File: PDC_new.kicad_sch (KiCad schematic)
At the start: 17 parts, among them J1 Conn_01x02, J10 Conn_01x02, J2 Conn_01x02, J3 Conn_01x02, J4 Conn_01x02, J5 Conn_01x02, J6 Conn_01x02, J7 Conn_01x02, J8 Conn_01x02, J9 Conn_01x02

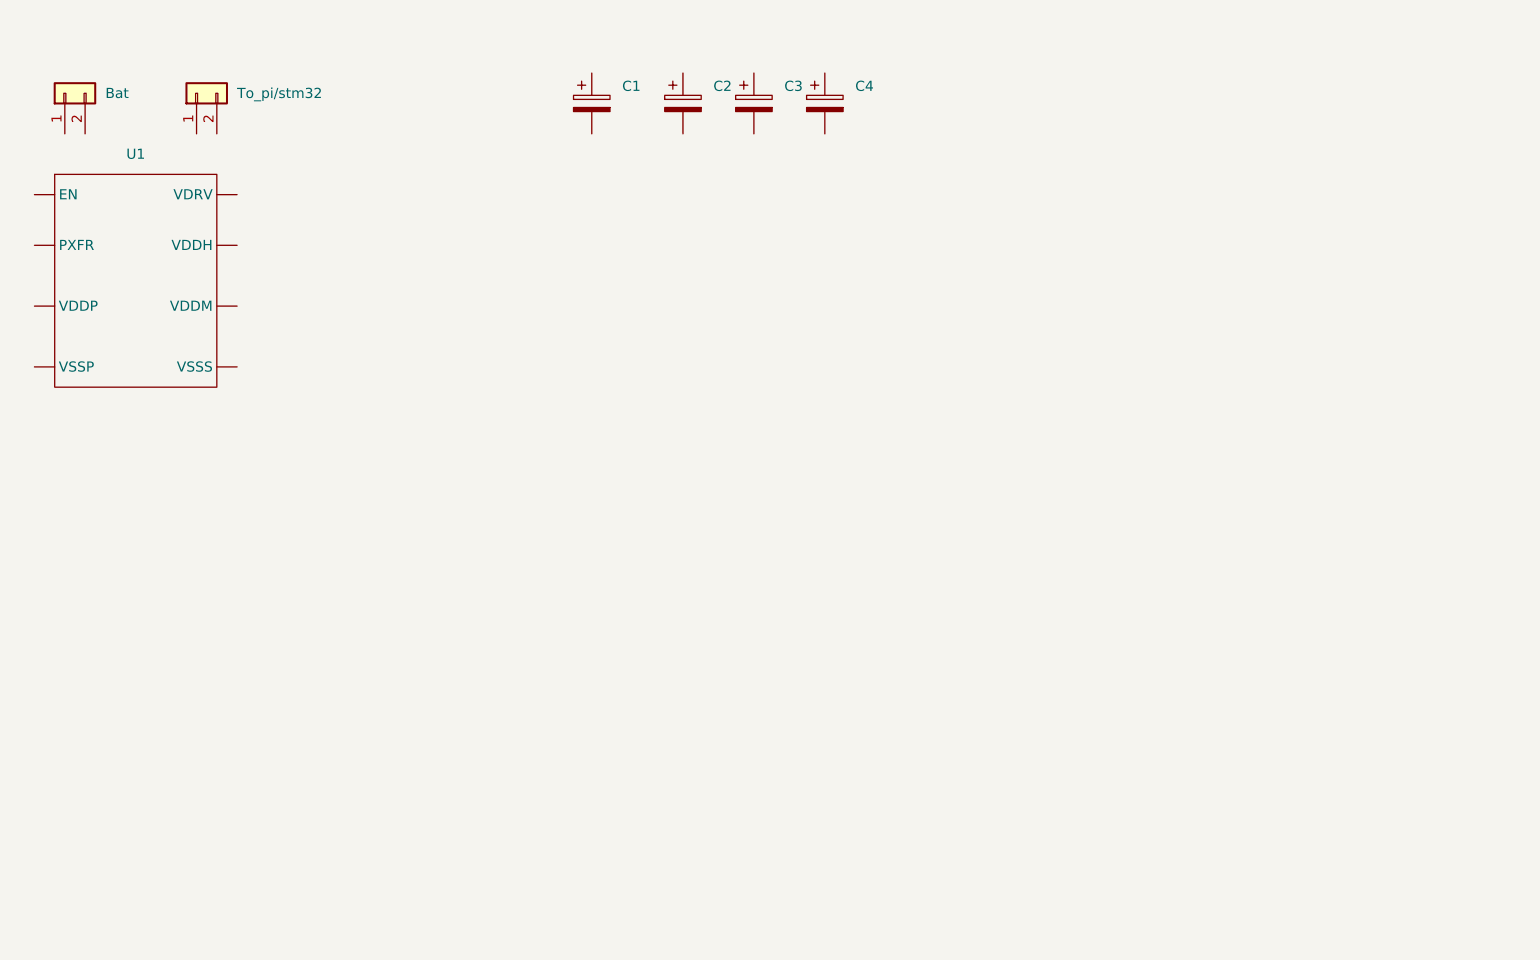
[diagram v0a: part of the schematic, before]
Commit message: Update PDC schematic with protection, timing and control logic
- Add XT90PW-F power input connector and SMCJ54CA-13-F TVS diode
- Add 3x TPSI3050-Q1 isolated switch drivers
- Add NE555 timer, LM393 comparator and 74HC14/74HC74/74LS08 logic
- Add Schottky diode and update connector/capacitor wiring
- Update project designators (C1-4, D1-2, J1-12, U1-8)

KiCad local files (.kicad_prl, backups, .history) remain ignored.

Co-Authored-By: Claude Opus 5.5 <noreply@anthropic.com>
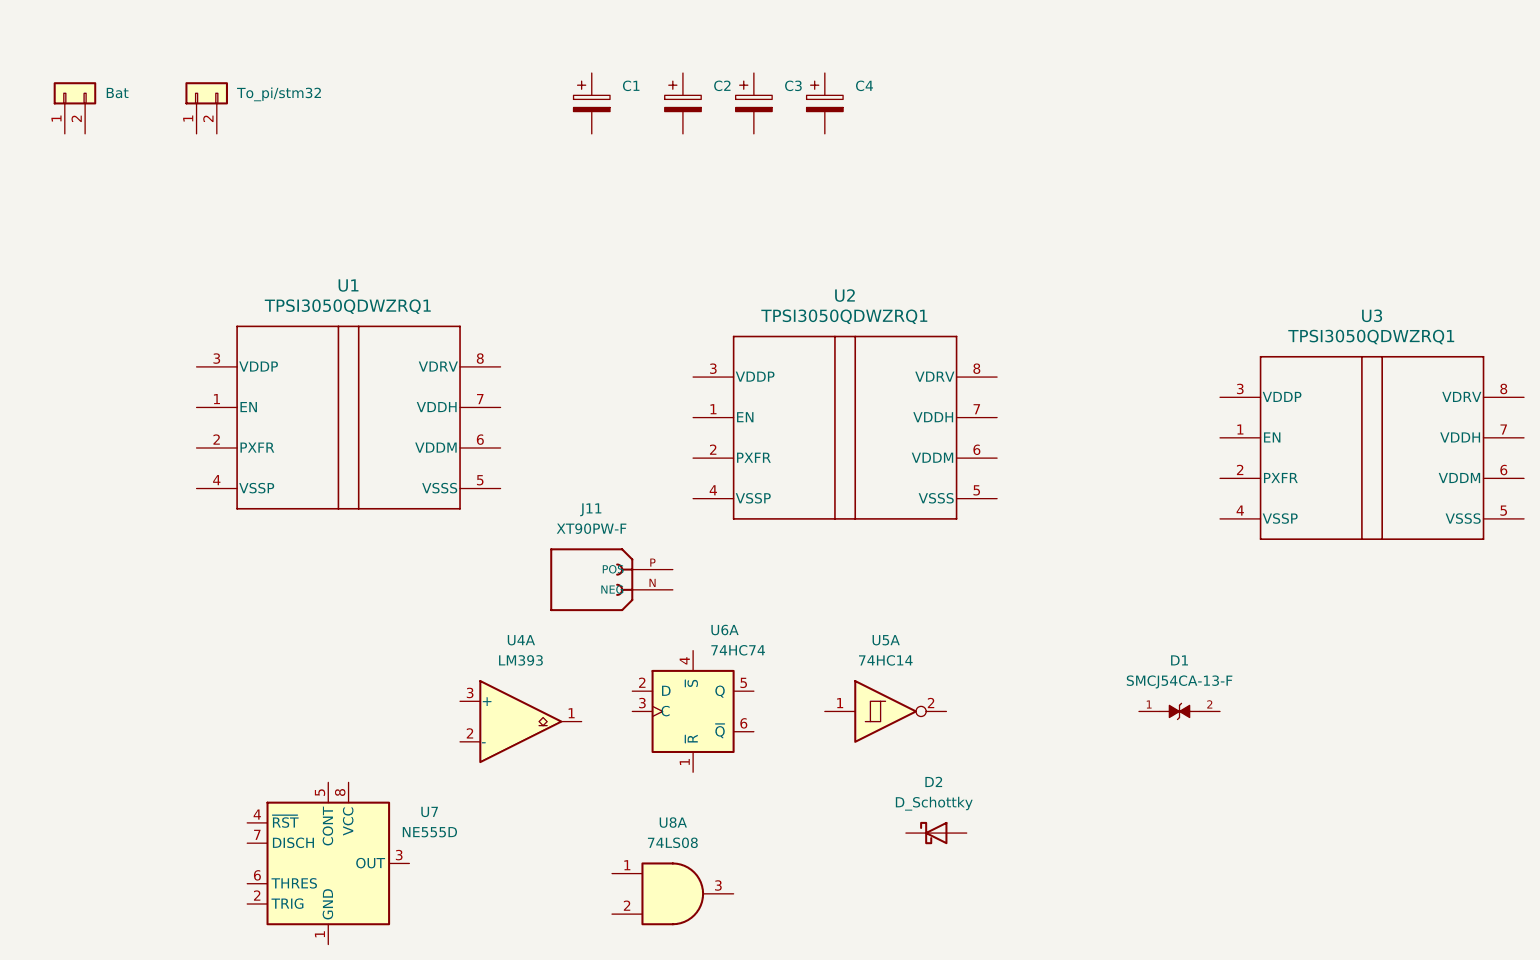
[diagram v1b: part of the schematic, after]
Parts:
- removed U1: (no value), TPSI3050-Q1:SOIC-8_DWZ_7.5x5.85mm_P1.27mm, symbol TPSI3050-Q1:_1
- added D1: SMCJ54CA-13-F, SMCJ54CA-13-F:TVS_SMCJ54CA-13-F, symbol SMCJ54CA:SMCJ54CA-13-F
- added D2: D_Schottky, symbol Device:D_Schottky
- added J11: XT90PW-F, XT90PW-F:AMASS_XT90PW-F, symbol XT90I:XT90PW-F
- added U1, U2, U3: TPSI3050QDWZRQ1, TPSI3050_Q1:DWZ0008A-MFG, symbol TPSI3050_Q1:TPSI3050QDWZRQ1
- added U4: LM393, symbol Comparator:LM393
- added U5: 74HC14, symbol 74xx:74HC14
- added U6: 74HC74, symbol 74xx:74HC74
- added U7: NE555D, Package_SO:SOIC-8_3.9x4.9mm_P1.27mm, symbol Timer:NE555D
- added U8: 74LS08, symbol 74xx:74LS08

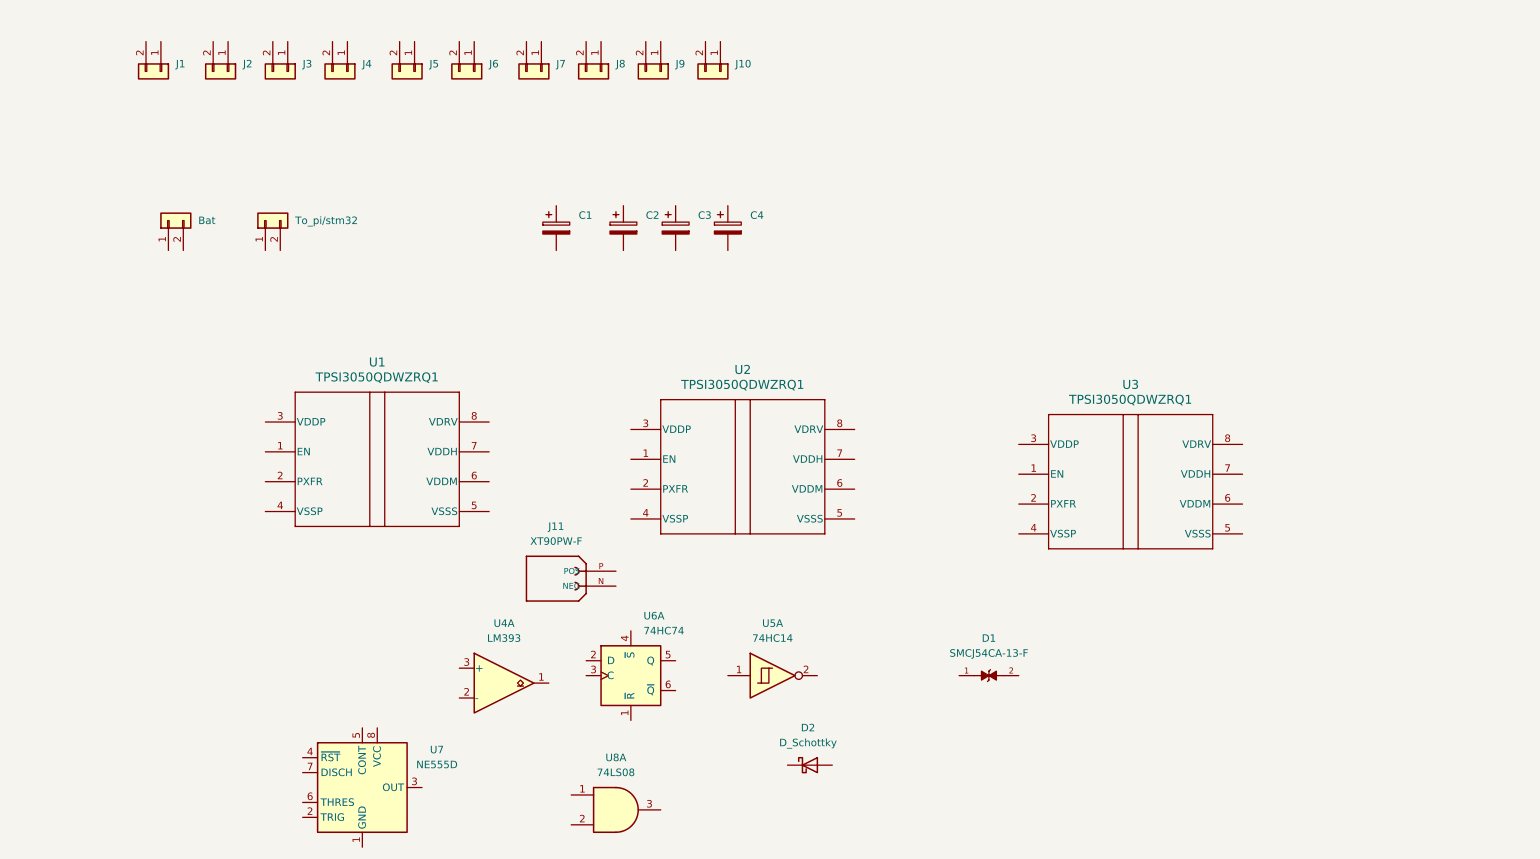
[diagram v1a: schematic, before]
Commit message: Update PDC schematic and add URB4805LD-60WR3 DC-DC converter library
Co-Authored-By: Claude Opus 5.5 <noreply@anthropic.com>
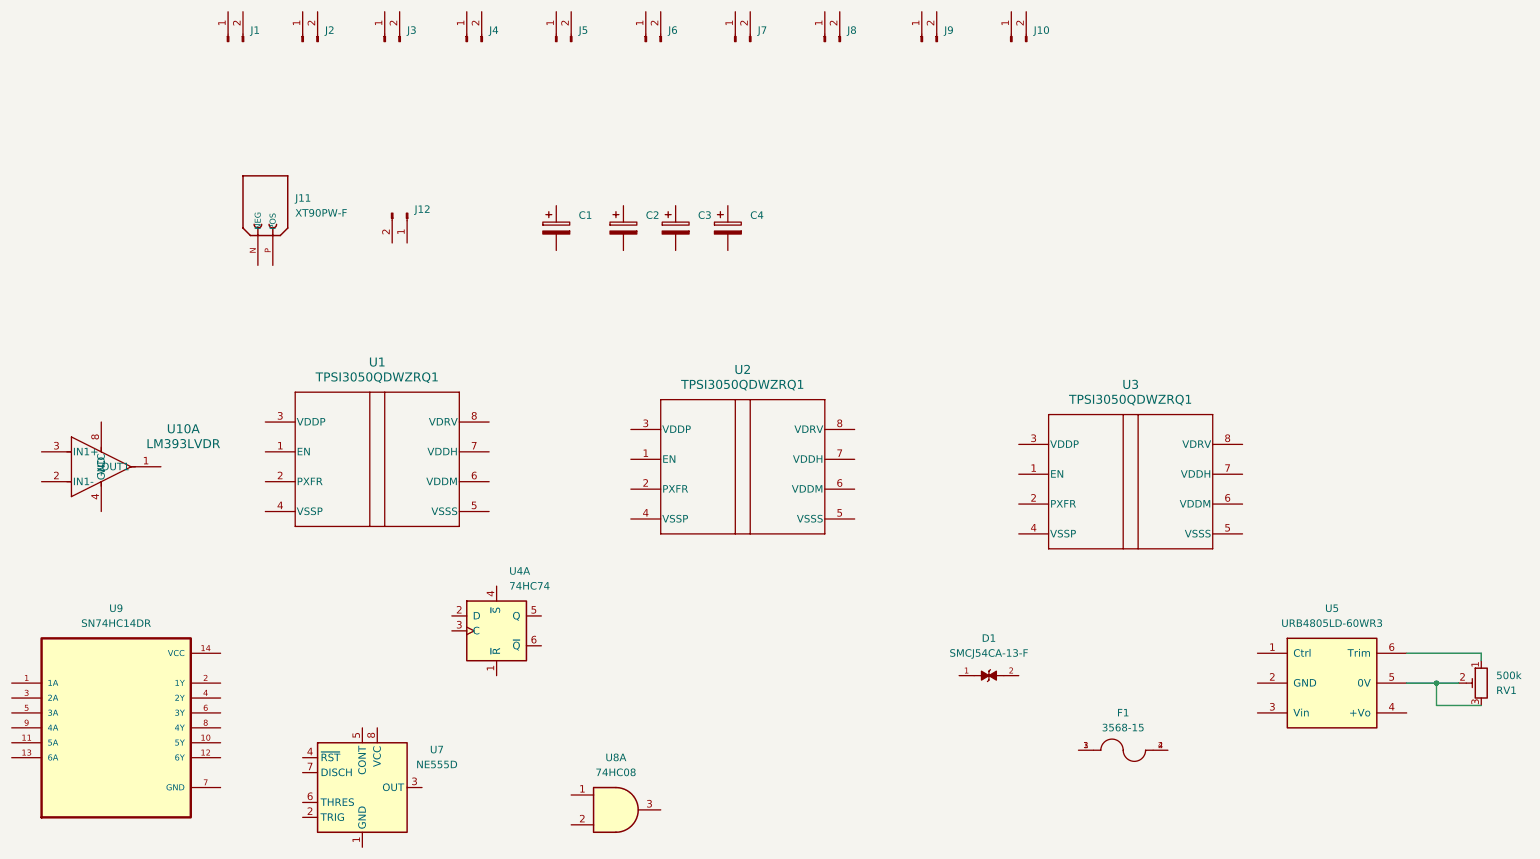
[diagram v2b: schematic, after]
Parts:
- removed Bat, J1, J10, J2, J3, J4, J5, J6, J7, J8, J9, To_pi/stm32: Conn_01x02, symbol Connector_Generic:Conn_01x02
- removed D2: D_Schottky, symbol Device:D_Schottky
- removed U4: LM393, symbol Comparator:LM393
- removed U5: 74HC14, symbol 74xx:74HC14
- removed U6: 74HC74, symbol 74xx:74HC74
- added F1: 3568-15, fuse:FUSE_3568-15, symbol 3568-15:3568-15
- added J1, J10, J2, J3, J4, J5, J6, J7, J8, J9: Conn_01x02_Pin, Connector_AMASS:AMASS_XT60PW-F_1x02_P7.20mm_Horizontal, symbol Connector:Conn_01x02_Pin
- added J12: Conn_01x02_Pin, Connector_AMASS:AMASS_XT30PW-F_1x02_P2.50mm_Horizontal, symbol Connector:Conn_01x02_Pin
- added RV1: 500k, Potentiometer_THT:Potentiometer_Bourns_3296W_Vertical, symbol Device:R_Potentiometer_Trim
- added U10: LM393LVDR, D0008A-IPC_A, symbol LM393LVDR:LM393LVDR
- added U4: 74HC74, Package_SO:SOIC-14_3.9x8.7mm_P1.27mm, symbol 74xx:74HC74
- added U5: URB4805LD-60WR3, NexusPDB:URB4805LD-60WR3, symbol URB48_LD-60WR3:URB4805LD-60WR3
- added U9: SN74HC14DR, SN74HC14DR:SOIC127P600X175-14N, symbol SN74HC14DR:SN74HC14DR
- U8: value 74LS08 -> 74HC08; footprint (none) -> Package_SO:SOIC-14_3.9x8.7mm_P1.27mm
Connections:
- new net: RV1.2, RV1.3, U5.5 (0V)
- new net: RV1.1, U5.6 (Trim)
- new net: F1.1, F1.3
- new net: F1.2, F1.4
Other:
- moved on the sheet: J11
